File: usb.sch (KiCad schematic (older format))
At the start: 1 part, among them CON1 BUQ2-USB-MICRO-B

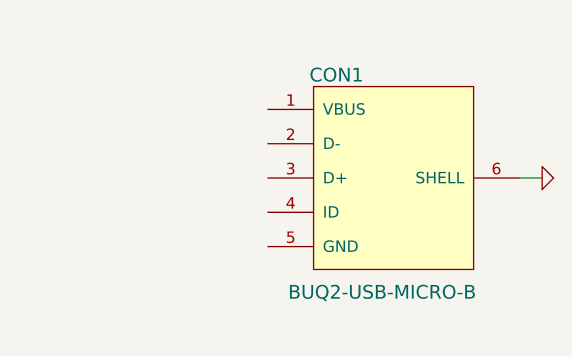
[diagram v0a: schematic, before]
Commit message: Add gps
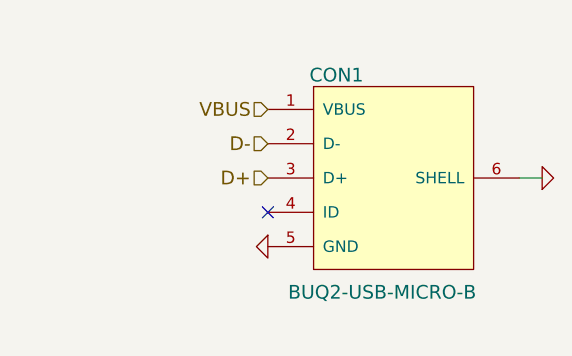
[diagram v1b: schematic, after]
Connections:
- net GND: now also CON1.5 (GND)
- net VBUS: now reaches CON1.1 (VBUS)
- net D-: now reaches CON1.2 (D-)
- net D+: now reaches CON1.3 (D+)
- no-connect marks 0 -> 1
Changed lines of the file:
@@
 $Descr A4 11693 8268
 encoding utf-8
-Sheet 6 10
+Sheet 6 11
 Title ""
 Date ""
@@
 $EndComp
 $Comp
-L GND #PWR10
+L GND #PWR16
 U 1 1 54463415
 P 5300 2550
-F 0 "#PWR10" H 5300 2550 30  0001 C CNN
+F 0 "#PWR16" H 5300 2550 30  0001 C CNN
 F 1 "GND" H 5300 2480 30  0001 C CNN
 F 2 "" H 5300 2550 60  0000 C CNN
@@
 Wire Wire Line
 	5300 2550 5200 2550
+$Comp
+L GND #PWR15
+U 1 1 546106F2
+P 4100 2850
+F 0 "#PWR15" H 4100 2850 30  0001 C CNN
+F 1 "GND" H 4100 2780 30  0001 C CNN
+F 2 "" H 4100 2850 60  0000 C CNN
+F 3 "" H 4100 2850 60  0000 C CNN
+	1    4100 2850
+	0    1    1    0
+$EndComp
+Text HLabel 4100 2250 0    60   Input ~ 0
+VBUS
+Text HLabel 4100 2400 0    60   Input ~ 0
+D-
+Text HLabel 4100 2550 0    60   Input ~ 0
+D+
+NoConn ~ 4100 2700
 $EndSCHEMATC

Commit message: More connections
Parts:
- CON1: footprint (none) -> buq2:USB-MICRO-B-FCI-10118194
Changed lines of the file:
@@
 F 0 "CON1" H 4400 3000 60  0000 C CNN
 F 1 "BUQ2-USB-MICRO-B" H 4600 2050 60  0000 C CNN
-F 2 "" H 4700 1850 60  0001 C CNN
+F 2 "buq2:USB-MICRO-B-FCI-10118194" H 4700 1850 60  0001 C CNN
 F 3 "http://portal.fciconnect.com/Comergent//fci/drawing/10118193.pdf" H 5100 1950 60  0001 C CNN
 F 4 "609-4616-1-ND" H 4800 3100 60  0001 C CNN "Digikey"
@@
 $EndComp
 $Comp
-L GND #PWR16
+L GND #PWR017
 U 1 1 54463415
 P 5300 2550
-F 0 "#PWR16" H 5300 2550 30  0001 C CNN
+F 0 "#PWR017" H 5300 2550 30  0001 C CNN
 F 1 "GND" H 5300 2480 30  0001 C CNN
 F 2 "" H 5300 2550 60  0000 C CNN
@@
 	5300 2550 5200 2550
 $Comp
-L GND #PWR15
+L GND #PWR018
 U 1 1 546106F2
 P 4100 2850
-F 0 "#PWR15" H 4100 2850 30  0001 C CNN
+F 0 "#PWR018" H 4100 2850 30  0001 C CNN
 F 1 "GND" H 4100 2780 30  0001 C CNN
 F 2 "" H 4100 2850 60  0000 C CNN

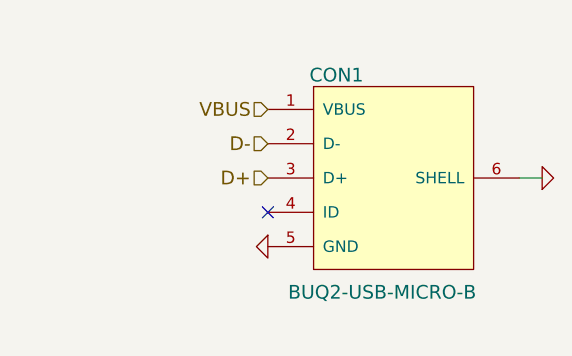
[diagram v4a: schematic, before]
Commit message: Add buttons. Fix DRC. Add antenna
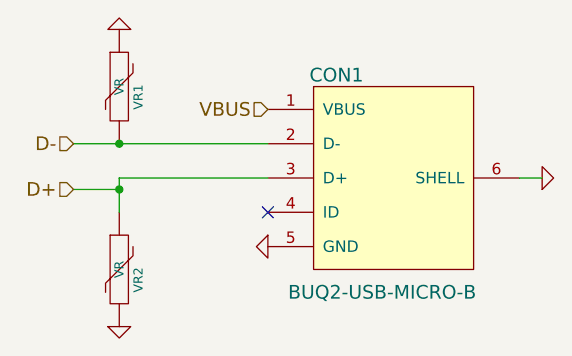
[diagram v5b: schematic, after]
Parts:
- added VR1, VR2: VR, symbol VR
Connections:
- net D+: now also VR2.1
- net D-: now also VR1.2
- net GND: now also VR1.1, VR2.2
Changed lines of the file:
@@
 $Descr A4 11693 8268
 encoding utf-8
-Sheet 6 13
+Sheet 6 14
 Title ""
 Date ""
@@
 $EndComp
 $Comp
-L GND #PWR018
+L GND #PWR019
 U 1 1 54463415
 P 5300 2550
-F 0 "#PWR018" H 5300 2550 30  0001 C CNN
+F 0 "#PWR019" H 5300 2550 30  0001 C CNN
 F 1 "GND" H 5300 2480 30  0001 C CNN
 F 2 "" H 5300 2550 60  0000 C CNN
@@
 	5300 2550 5200 2550
 $Comp
-L GND #PWR019
+L GND #PWR020
 U 1 1 546106F2
 P 4100 2850
-F 0 "#PWR019" H 4100 2850 30  0001 C CNN
+F 0 "#PWR020" H 4100 2850 30  0001 C CNN
 F 1 "GND" H 4100 2780 30  0001 C CNN
 F 2 "" H 4100 2850 60  0000 C CNN
@@
 Text HLabel 4100 2250 0    60   Input ~ 0
 VBUS
-Text HLabel 4100 2400 0    60   Input ~ 0
+Text HLabel 3250 2400 0    60   Input ~ 0
 D-
-Text HLabel 4100 2550 0    60   Input ~ 0
+Text HLabel 3250 2600 0    60   Input ~ 0
 D+
 NoConn ~ 4100 2700
+$Comp
+L VR VR2
+U 1 1 54648C4F
+P 3450 2950
+F 0 "VR2" V 3510 2904 40  0000 C TNN
+F 1 "VR" V 3450 2950 40  0000 C CNN
+F 2 "" H 3450 2950 60  0000 C CNN
+F 3 "" H 3450 2950 60  0000 C CNN
+	1    3450 2950
+	1    0    0    -1
+$EndComp
+$Comp
+L VR VR1
+U 1 1 54648D2E
+P 3450 2150
+F 0 "VR1" V 3510 2104 40  0000 C TNN
+F 1 "VR" V 3450 2150 40  0000 C CNN
+F 2 "" H 3450 2150 60  0000 C CNN
+F 3 "" H 3450 2150 60  0000 C CNN
+	1    3450 2150
+	1    0    0    -1
+$EndComp
+Wire Wire Line
+	4100 2550 3450 2550
+Wire Wire Line
+	3450 2550 3450 2700
+Wire Wire Line
+	3450 2600 3250 2600
+Wire Wire Line
+	3250 2400 4100 2400
+Connection ~ 3450 2400
+Connection ~ 3450 2600
+$Comp
+L GND #PWR021
+U 1 1 54648DE0
+P 3450 3200
+F 0 "#PWR021" H 3450 3200 30  0001 C CNN
+F 1 "GND" H 3450 3130 30  0001 C CNN
+F 2 "" H 3450 3200 60  0000 C CNN
+F 3 "" H 3450 3200 60  0000 C CNN
+	1    3450 3200
+	1    0    0    -1
+$EndComp
+$Comp
+L GND #PWR022
+U 1 1 54648DF7
+P 3450 1900
+F 0 "#PWR022" H 3450 1900 30  0001 C CNN
+F 1 "GND" H 3450 1830 30  0001 C CNN
+F 2 "" H 3450 1900 60  0000 C CNN
+F 3 "" H 3450 1900 60  0000 C CNN
+	1    3450 1900
+	-1   0    0    1
+$EndComp
 $EndSCHEMATC

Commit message: Start first layout test
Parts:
- VR1, VR2: footprint (none) -> buq2:SM0603
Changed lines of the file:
@@
 F 0 "VR2" V 3510 2904 40  0000 C TNN
 F 1 "VR" V 3450 2950 40  0000 C CNN
-F 2 "" H 3450 2950 60  0000 C CNN
+F 2 "buq2:SM0603" H 3450 2950 60  0001 C CNN
 F 3 "" H 3450 2950 60  0000 C CNN
 	1    3450 2950
@@
 F 0 "VR1" V 3510 2104 40  0000 C TNN
 F 1 "VR" V 3450 2150 40  0000 C CNN
-F 2 "" H 3450 2150 60  0000 C CNN
+F 2 "buq2:SM0603" H 3450 2150 60  0001 C CNN
 F 3 "" H 3450 2150 60  0000 C CNN
 	1    3450 2150
